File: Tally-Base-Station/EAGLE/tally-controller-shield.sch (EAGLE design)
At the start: 27 parts, among them J2 Mega R3, U1 SN75174N, U2 SN75174N, U3 SN75174N

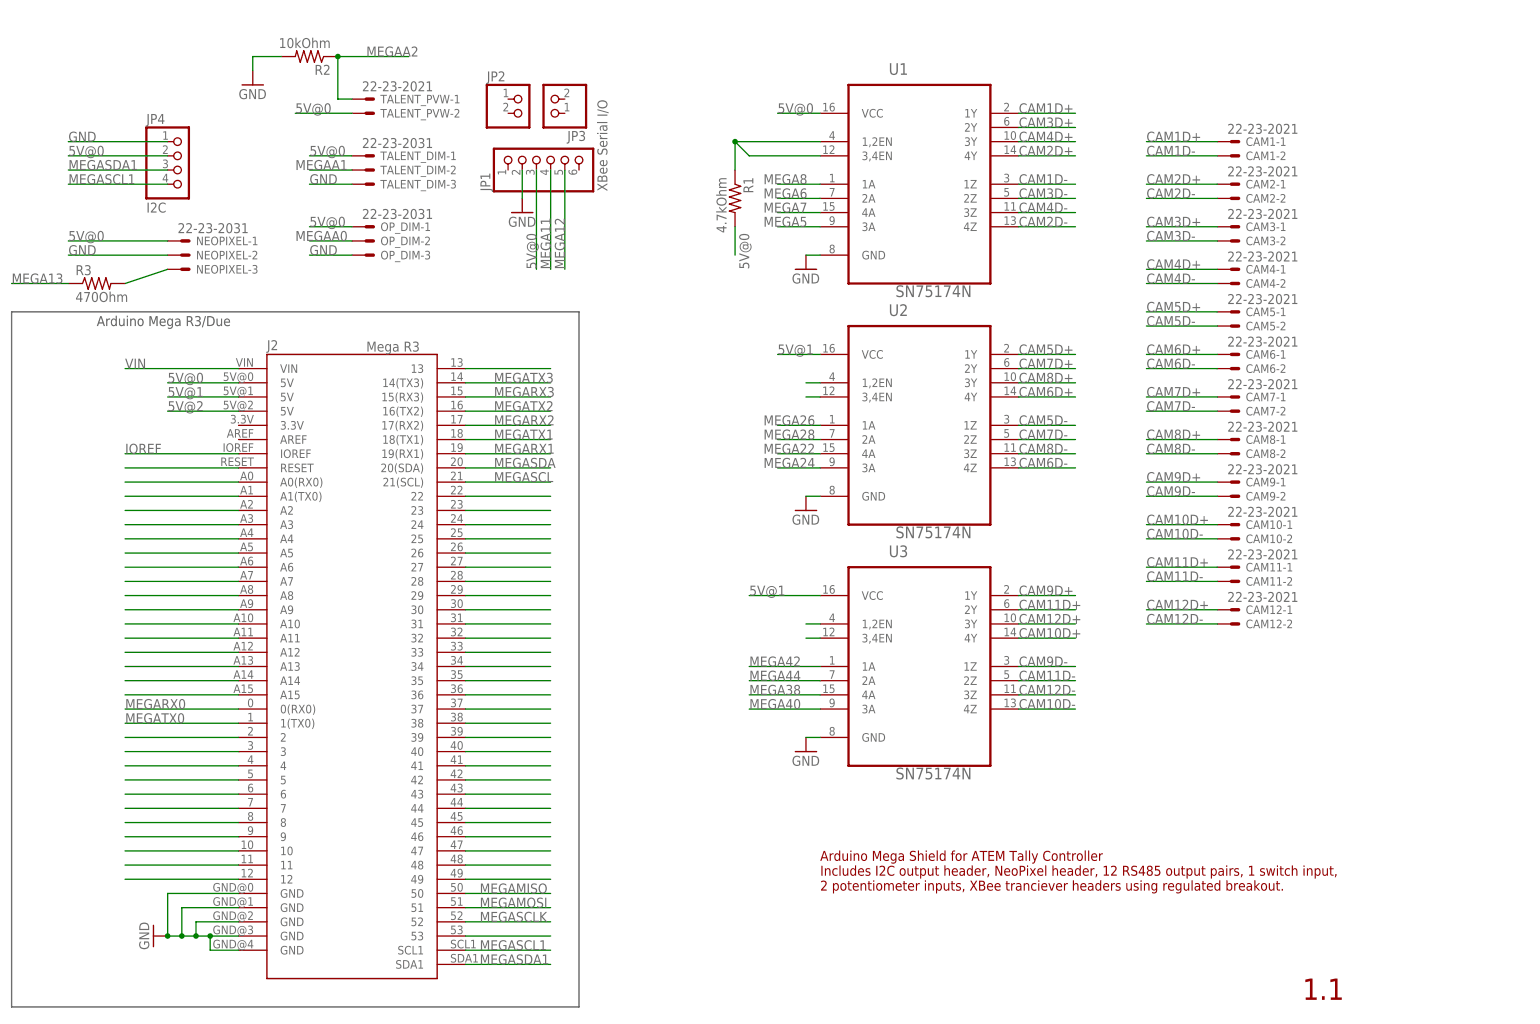
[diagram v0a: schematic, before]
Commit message: Standardize RS485 pinouts, update RJ45 pinouts.
Fix pin assignments for the RS485 interconnects to standardize on pin1 = data-.
Update the RJ45 breakouts to be mostly pin compatible with DMX over ethernet wiring standard (using pin 5/6 for V+)
Create an XLR RS485 breakout option for wiring cameras together using 3pin DMX cables
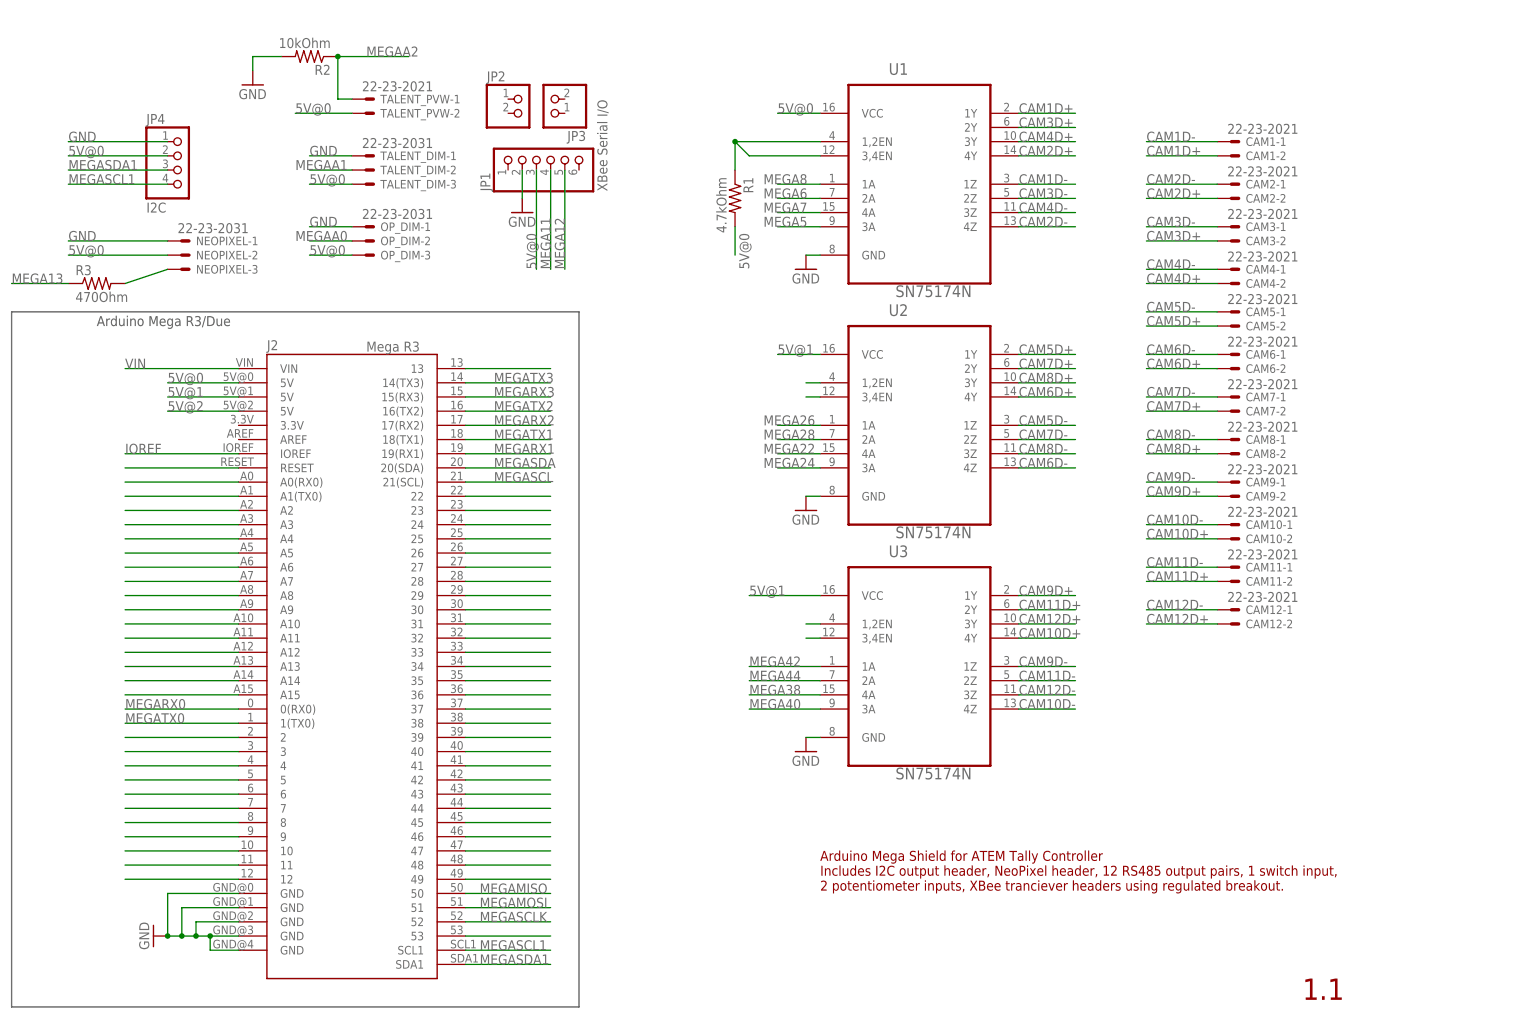
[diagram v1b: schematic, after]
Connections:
- net 5V@0: now also NEOPIXEL-2.S, OP_DIM-3.S, TALENT_DIM-3.S; no longer NEOPIXEL-1.S, OP_DIM-1.S, TALENT_DIM-1.S
- net CAM10D+: now also CAM10-2.S; no longer CAM10-1.S
- net CAM10D-: now also CAM10-1.S; no longer CAM10-2.S
- net CAM11D+: now also CAM11-2.S; no longer CAM11-1.S
- net CAM11D-: now also CAM11-1.S; no longer CAM11-2.S
- net CAM12D+: now also CAM12-2.S; no longer CAM12-1.S
- net CAM12D-: now also CAM12-1.S; no longer CAM12-2.S
- net CAM1D+: now also CAM1-2.S; no longer CAM1-1.S
- net CAM1D-: now also CAM1-1.S; no longer CAM1-2.S
- net CAM2D+: now also CAM2-2.S; no longer CAM2-1.S
- net CAM2D-: now also CAM2-1.S; no longer CAM2-2.S
- net CAM3D+: now also CAM3-2.S; no longer CAM3-1.S
- net CAM3D-: now also CAM3-1.S; no longer CAM3-2.S
- net CAM4D+: now also CAM4-2.S; no longer CAM4-1.S
- net CAM4D-: now also CAM4-1.S; no longer CAM4-2.S
- net CAM5D+: now also CAM5-2.S; no longer CAM5-1.S
- net CAM5D-: now also CAM5-1.S; no longer CAM5-2.S
- net CAM6D+: now also CAM6-2.S; no longer CAM6-1.S
- net CAM6D-: now also CAM6-1.S; no longer CAM6-2.S
- net CAM7D+: now also CAM7-2.S; no longer CAM7-1.S
- net CAM7D-: now also CAM7-1.S; no longer CAM7-2.S
- net CAM8D+: now also CAM8-2.S; no longer CAM8-1.S
- net CAM8D-: now also CAM8-1.S; no longer CAM8-2.S
- net CAM9D+: now also CAM9-2.S; no longer CAM9-1.S
- net CAM9D-: now also CAM9-1.S; no longer CAM9-2.S
- net GND: now also NEOPIXEL-1.S, OP_DIM-1.S, TALENT_DIM-1.S; no longer NEOPIXEL-2.S, OP_DIM-3.S, TALENT_DIM-3.S

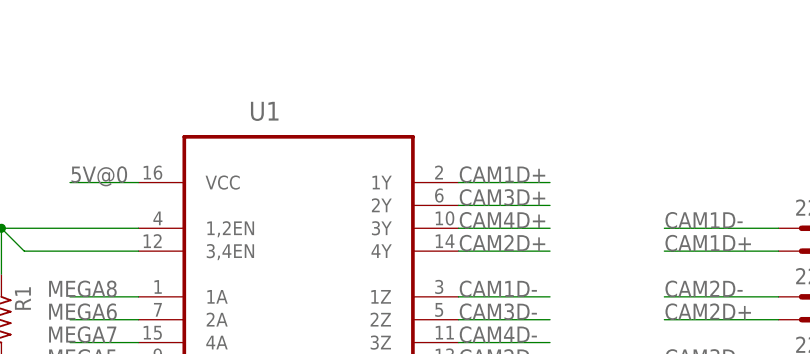
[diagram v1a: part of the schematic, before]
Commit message: Add notes to schematic.  Code cleanup of sketch.
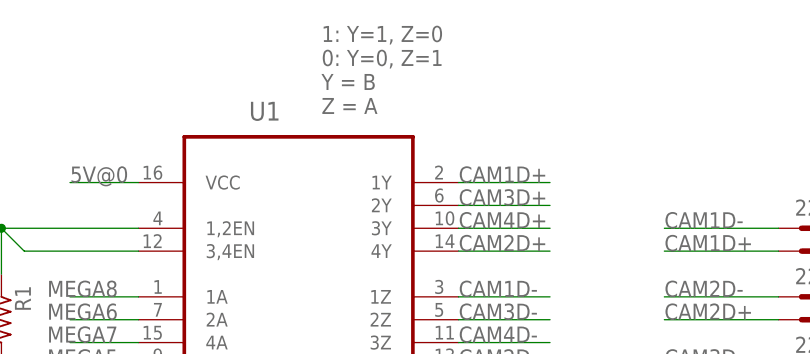
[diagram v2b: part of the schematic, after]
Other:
- note added: "1: Y=1, Z=0 0: Y=0, Z=1 Y = B Z = A"
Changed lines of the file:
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@@
 2 potentiometer inputs, XBee tranciever headers using regulated breakout.</text>
 <text x="71.12" y="-7.62" size="3.81" layer="94" align="top-left">1.1</text>
+<text x="5.08" y="154.94" size="1.778" layer="95">1: Y=1, Z=0
+0: Y=0, Z=1
+Y = B
+Z = A</text>
 </plain>
 <instances>
